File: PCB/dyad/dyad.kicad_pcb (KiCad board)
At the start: 2 copper layers, 7 parts, among them SW1 SW_SPST, SW2 SW_SPST, SW3 SW_SPST, SW4 SW_SPST, SW5 SW_SPST, SW6 SW_SPST

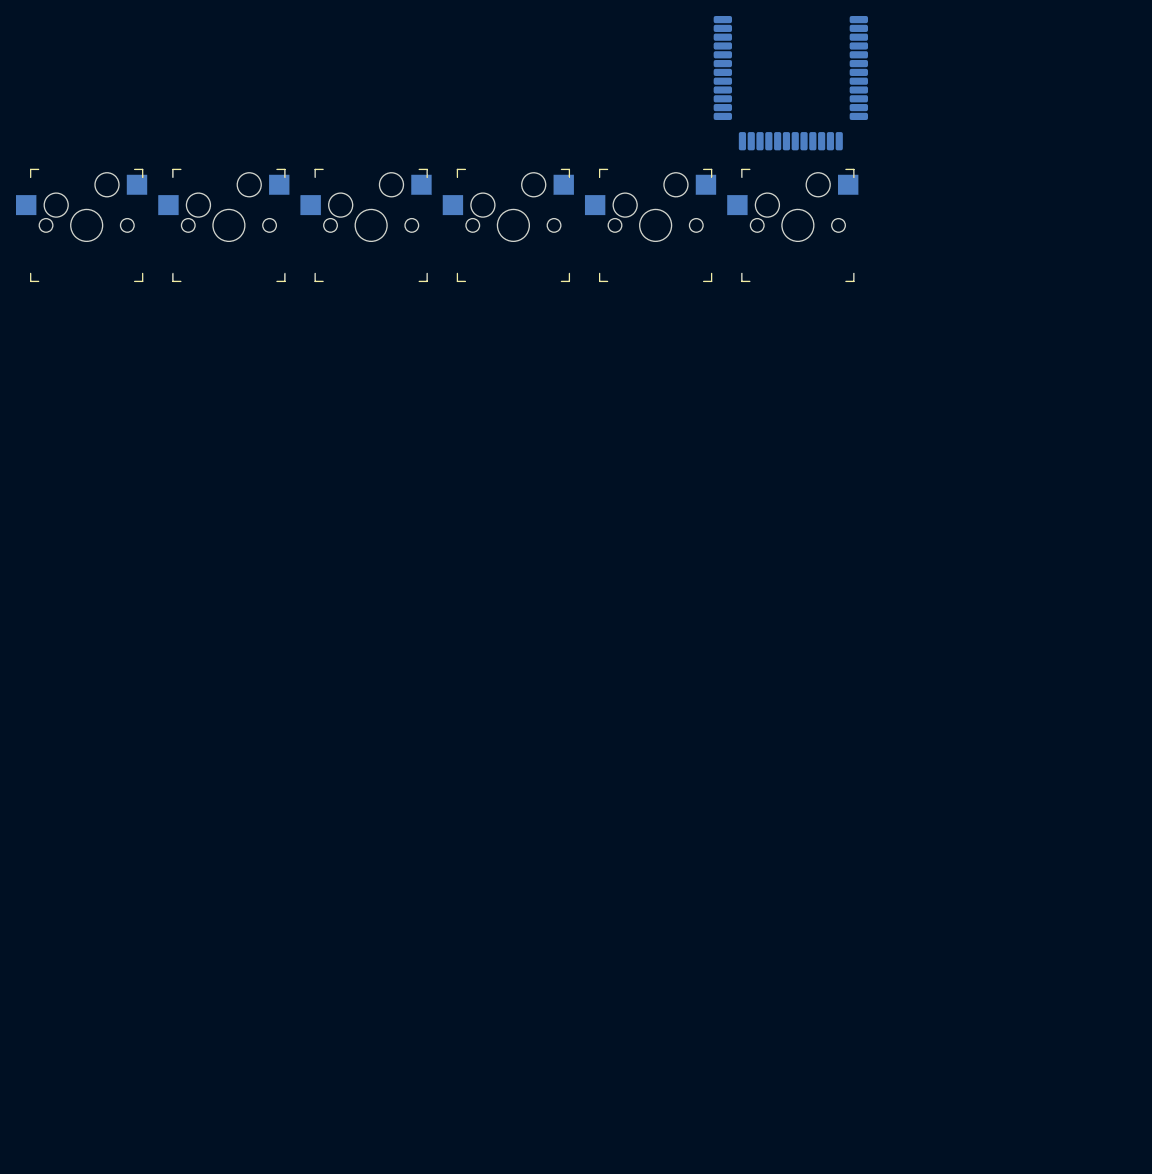
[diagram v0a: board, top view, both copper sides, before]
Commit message: add diodes
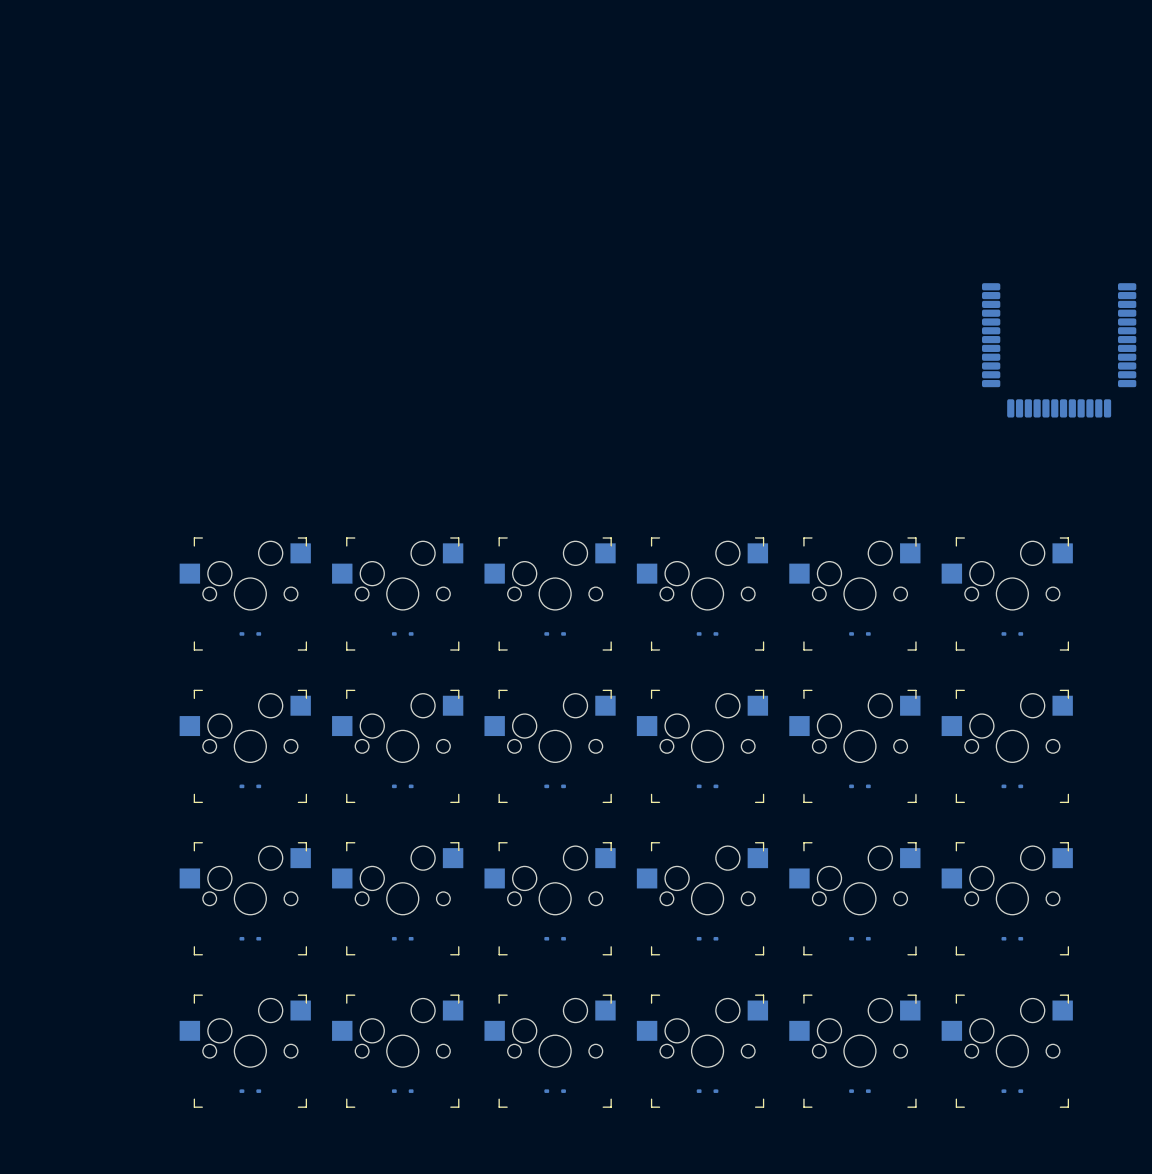
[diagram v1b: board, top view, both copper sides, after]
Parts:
- added D1: 1N4148WS, Diode_SMD:D_SOD-323, B.Cu at (48.4, 107.0)
- added D10: 1N4148WS, Diode_SMD:D_SOD-323, B.Cu at (105.5, 126.0)
- added D11: 1N4148WS, Diode_SMD:D_SOD-323, B.Cu at (124.6, 126.0)
- added D12: 1N4148WS, Diode_SMD:D_SOD-323, B.Cu at (143.7, 126.0)
- added D13: 1N4148WS, Diode_SMD:D_SOD-323, B.Cu at (48.4, 145.1)
- added D14: 1N4148WS, Diode_SMD:D_SOD-323, B.Cu at (67.5, 145.1)
- added D15: 1N4148WS, Diode_SMD:D_SOD-323, B.Cu at (86.5, 145.1)
- added D16: 1N4148WS, Diode_SMD:D_SOD-323, B.Cu at (105.5, 145.1)
- added D17: 1N4148WS, Diode_SMD:D_SOD-323, B.Cu at (124.6, 145.1)
- added D18: 1N4148WS, Diode_SMD:D_SOD-323, B.Cu at (143.7, 145.1)
- added D19: 1N4148WS, Diode_SMD:D_SOD-323, B.Cu at (48.4, 164.1)
- added D2: 1N4148WS, Diode_SMD:D_SOD-323, B.Cu at (67.5, 107.0)
- added D20: 1N4148WS, Diode_SMD:D_SOD-323, B.Cu at (67.5, 164.1)
- added D21: 1N4148WS, Diode_SMD:D_SOD-323, B.Cu at (86.5, 164.1)
- added D22: 1N4148WS, Diode_SMD:D_SOD-323, B.Cu at (105.5, 164.1)
- added D23: 1N4148WS, Diode_SMD:D_SOD-323, B.Cu at (124.6, 164.1)
- added D24: 1N4148WS, Diode_SMD:D_SOD-323, B.Cu at (143.7, 164.1)
- added D3: 1N4148WS, Diode_SMD:D_SOD-323, B.Cu at (86.5, 107.0)
- added D4: 1N4148WS, Diode_SMD:D_SOD-323, B.Cu at (105.5, 107.0)
- added D5: 1N4148WS, Diode_SMD:D_SOD-323, B.Cu at (124.6, 107.0)
- added D6: 1N4148WS, Diode_SMD:D_SOD-323, B.Cu at (143.7, 107.0)
- added D7: 1N4148WS, Diode_SMD:D_SOD-323, B.Cu at (48.4, 126.0)
- added D8: 1N4148WS, Diode_SMD:D_SOD-323, B.Cu at (67.5, 126.0)
- added D9: 1N4148WS, Diode_SMD:D_SOD-323, B.Cu at (86.5, 126.0)
- added SW10: SW_SPST, keyswitches.pretty-master:Kailh_socket_MX, F.Cu at (105.5, 121.0)
- added SW11: SW_SPST, keyswitches.pretty-master:Kailh_socket_MX, F.Cu at (124.6, 121.0)
- added SW12: SW_SPST, keyswitches.pretty-master:Kailh_socket_MX, F.Cu at (143.7, 121.0)
- added SW13: SW_SPST, keyswitches.pretty-master:Kailh_socket_MX, F.Cu at (48.4, 140.1)
- added SW14: SW_SPST, keyswitches.pretty-master:Kailh_socket_MX, F.Cu at (67.5, 140.1)
- added SW15: SW_SPST, keyswitches.pretty-master:Kailh_socket_MX, F.Cu at (86.5, 140.1)
- added SW16: SW_SPST, keyswitches.pretty-master:Kailh_socket_MX, F.Cu at (105.5, 140.1)
- added SW17: SW_SPST, keyswitches.pretty-master:Kailh_socket_MX, F.Cu at (124.6, 140.1)
- added SW18: SW_SPST, keyswitches.pretty-master:Kailh_socket_MX, F.Cu at (143.7, 140.1)
- added SW19: SW_SPST, keyswitches.pretty-master:Kailh_socket_MX, F.Cu at (48.4, 159.1)
- added SW20: SW_SPST, keyswitches.pretty-master:Kailh_socket_MX, F.Cu at (67.5, 159.1)
- added SW21: SW_SPST, keyswitches.pretty-master:Kailh_socket_MX, F.Cu at (86.5, 159.1)
- added SW22: SW_SPST, keyswitches.pretty-master:Kailh_socket_MX, F.Cu at (105.5, 159.1)
- added SW23: SW_SPST, keyswitches.pretty-master:Kailh_socket_MX, F.Cu at (124.6, 159.1)
- added SW24: SW_SPST, keyswitches.pretty-master:Kailh_socket_MX, F.Cu at (143.7, 159.1)
- added SW7: SW_SPST, keyswitches.pretty-master:Kailh_socket_MX, F.Cu at (48.4, 121.0)
- added SW8: SW_SPST, keyswitches.pretty-master:Kailh_socket_MX, F.Cu at (67.5, 121.0)
- added SW9: SW_SPST, keyswitches.pretty-master:Kailh_socket_MX, F.Cu at (86.5, 121.0)
- moved SW6 53.3 mm to (143.7, 102.0)
- moved SW5 52.7 mm to (124.6, 102.0)
- moved SW4 52.1 mm to (105.5, 102.0)
- moved SW3 51.5 mm to (86.5, 102.0)
- moved SW2 50.9 mm to (67.5, 102.0)
- moved SW1 50.4 mm to (48.4, 102.0)
- moved U1 47.3 mm to (158.0, 78.8)
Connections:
- SW1 pad 1: unconnected-(SW1-A-Pad1) -> ROW0
- SW1 pad 2: unconnected-(SW1-B-Pad2) -> Net-(D1-A)
- SW2 pad 1: unconnected-(SW2-A-Pad1) -> ROW0
- SW2 pad 2: unconnected-(SW2-B-Pad2) -> Net-(D2-A)
- SW3 pad 1: unconnected-(SW3-A-Pad1) -> ROW0
- SW3 pad 2: unconnected-(SW3-B-Pad2) -> Net-(D3-A)
- SW4 pad 1: unconnected-(SW4-A-Pad1) -> ROW0
- SW4 pad 2: unconnected-(SW4-B-Pad2) -> Net-(D4-A)
- SW5 pad 1: unconnected-(SW5-A-Pad1) -> ROW0
- SW5 pad 2: unconnected-(SW5-B-Pad2) -> Net-(D5-A)
- SW6 pad 1: unconnected-(SW6-A-Pad1) -> ROW0
- SW6 pad 2: unconnected-(SW6-B-Pad2) -> Net-(D6-A)

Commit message: added mounting holes
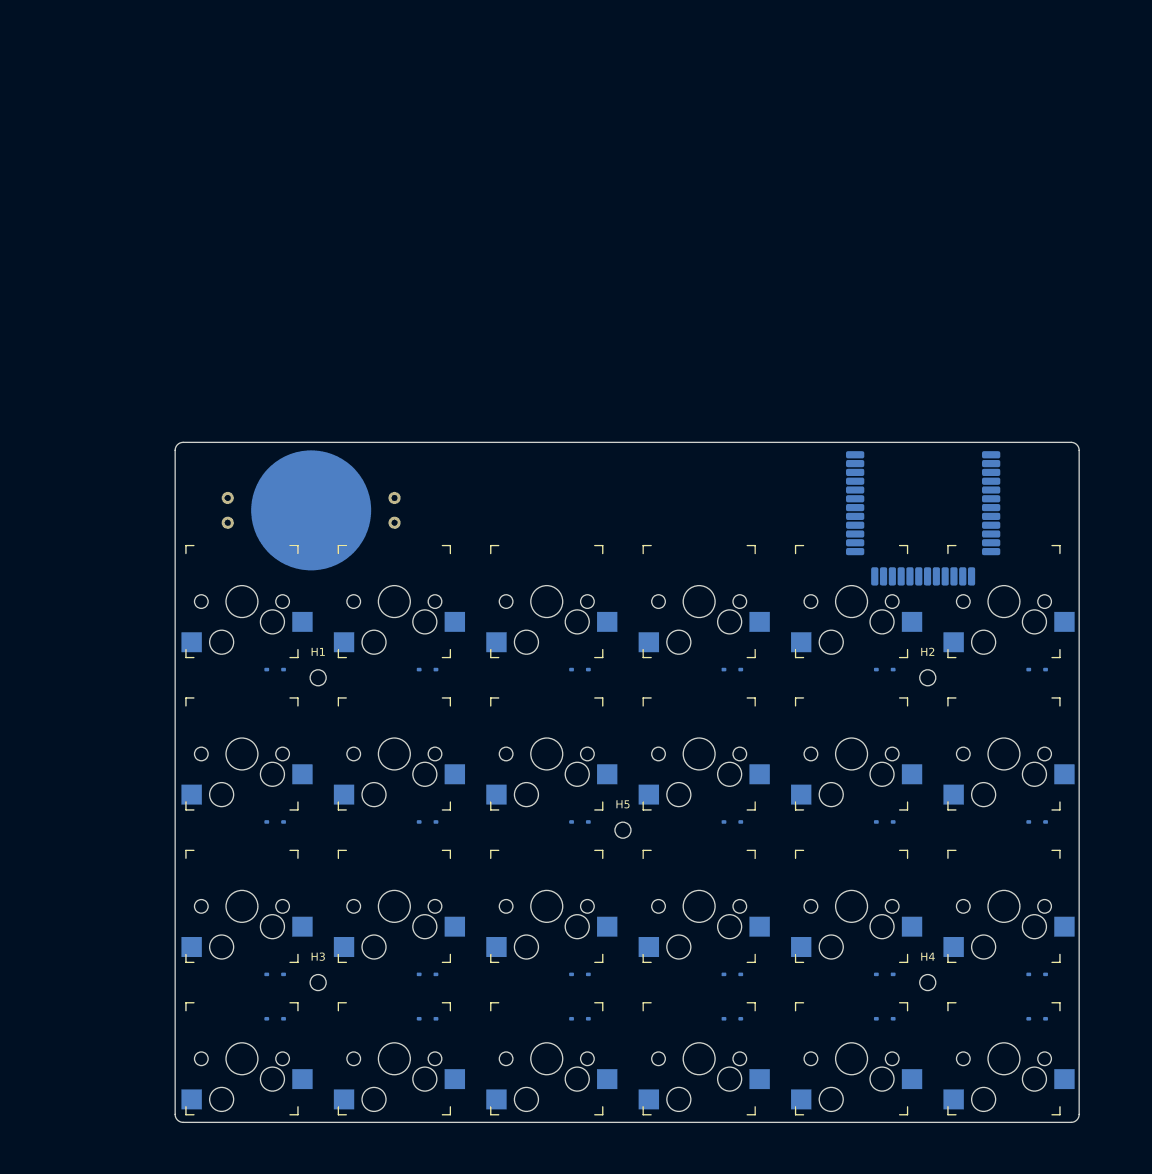
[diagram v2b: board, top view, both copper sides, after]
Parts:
- added BT1: Battery_Cell, lcsc:MY-2032-31, B.Cu at (56.0, 91.5)
- added H1: MountingHole, MountingHole:MountingHole_2mm, F.Cu at (56.9, 112.4)
- added H2: MountingHole, MountingHole:MountingHole_2mm, F.Cu at (133.1, 112.4)
- added H3: MountingHole, MountingHole:MountingHole_2mm, F.Cu at (56.9, 150.5)
- added H4: MountingHole, MountingHole:MountingHole_2mm, F.Cu at (133.1, 150.5)
- added H5: MountingHole, MountingHole:MountingHole_2mm, F.Cu at (95.0, 131.5)
- moved SW6 112.5 mm to (47.4, 160.1), turned to 180 degrees
- moved D19 111.6 mm to (146.8, 111.4), turned to 0 degrees
- moved SW24 111.5 mm to (47.4, 102.9), turned to 180 degrees
- moved SW1 110.7 mm to (142.6, 160.1), turned to 180 degrees
- moved SW19 109.7 mm to (142.6, 102.9), turned to 180 degrees
- moved D1 109.5 mm to (146.8, 155.1), turned to 0 degrees
- moved D24 106.2 mm to (51.5, 111.4), turned to 0 degrees
- moved D6 103.9 mm to (51.5, 155.1), turned to 0 degrees
- moved D7 101.1 mm to (146.8, 149.5), turned to 0 degrees
- moved D13 99.4 mm to (146.8, 130.4), turned to 0 degrees
- moved SW12 98.4 mm to (47.4, 141.0), turned to 180 degrees
- moved SW18 98.0 mm to (47.4, 122.0), turned to 180 degrees
- moved SW7 96.3 mm to (142.6, 141.0), turned to 180 degrees
- moved SW13 95.9 mm to (142.6, 122.0), turned to 180 degrees
- moved D12 95.1 mm to (51.5, 149.5), turned to 0 degrees
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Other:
- board outline added: 113 x 85 mm

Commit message: update pcb and schematic
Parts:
- added CHG1: Conn_01x04_Pin, Connector_PinHeader_2.54mm:PinHeader_1x04_P2.54mm_Vertical, F.Cu at (83.4, 88.8)
- added PRG1: Conn_01x04_Pin, Connector_PinHeader_2.54mm:PinHeader_1x04_P2.54mm_Vertical, F.Cu at (146.2, 85.8)
- moved BT1 1.09 mm to (56.9, 92.0)
- renumbered D24 to D1, D15 to D10, D14 to D11, D13 to D12, D12 to D13, D11 to D14, D10 to D15, D9 to D16, D8 to D17, D7 to D18, D6 to D19, D23 to D2, D5 to D20, D4 to D21, D3 to D22, D2 to D23, D1 to D24, D22 to D3, D21 to D4, D20 to D5, D19 to D6, D18 to D7, D17 to D8, D16 to D9, SW24 to SW1, SW15 to SW10, SW14 to SW11, SW13 to SW12, SW12 to SW13, SW11 to SW14, SW10 to SW15, SW9 to SW16, SW8 to SW17, SW7 to SW18, SW6 to SW19, SW23 to SW2, SW5 to SW20, SW4 to SW21, SW3 to SW22, SW2 to SW23, SW1 to SW24, SW22 to SW3, SW21 to SW4, SW20 to SW5, SW19 to SW6, SW18 to SW7, SW17 to SW8, SW16 to SW9
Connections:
- D1 pad 1: COL5 -> COL0
- D10 pad 1: COL2 -> COL3
- D11 pad 1: COL1 -> COL4
- D12 pad 1: COL0 -> COL5
- D13 pad 1: COL5 -> COL0
- D14 pad 1: COL4 -> COL1
- D15 pad 1: COL3 -> COL2
- D16 pad 1: COL2 -> COL3
- D17 pad 1: COL1 -> COL4
- D18 pad 1: COL0 -> COL5
- D19 pad 1: COL5 -> COL0
- D2 pad 1: COL4 -> COL1
- D20 pad 1: COL4 -> COL1
- D21 pad 1: COL3 -> COL2
- D22 pad 1: COL2 -> COL3
- D23 pad 1: COL1 -> COL4
- D24 pad 1: COL0 -> COL5
- D3 pad 1: COL3 -> COL2
- D4 pad 1: COL2 -> COL3
- D5 pad 1: COL1 -> COL4
- D6 pad 1: COL0 -> COL5
- D7 pad 1: COL5 -> COL0
- D8 pad 1: COL4 -> COL1
- D9 pad 1: COL3 -> COL2
- SW1 pad 1: ROW3 -> ROW0
- SW10 pad 1: ROW2 -> ROW1
- SW11 pad 1: ROW2 -> ROW1
- SW12 pad 1: ROW2 -> ROW1
- SW13 pad 1: ROW1 -> ROW2
- SW14 pad 1: ROW1 -> ROW2
- SW15 pad 1: ROW1 -> ROW2
- SW16 pad 1: ROW1 -> ROW2
- SW17 pad 1: ROW1 -> ROW2
- SW18 pad 1: ROW1 -> ROW2
- SW19 pad 1: ROW0 -> ROW3
- SW2 pad 1: ROW3 -> ROW0
- SW20 pad 1: ROW0 -> ROW3
- SW21 pad 1: ROW0 -> ROW3
- SW22 pad 1: ROW0 -> ROW3
- SW23 pad 1: ROW0 -> ROW3
- SW24 pad 1: ROW0 -> ROW3
- SW3 pad 1: ROW3 -> ROW0
- SW4 pad 1: ROW3 -> ROW0
- SW5 pad 1: ROW3 -> ROW0
- SW6 pad 1: ROW3 -> ROW0
- SW7 pad 1: ROW2 -> ROW1
- SW8 pad 1: ROW2 -> ROW1
- SW9 pad 1: ROW2 -> ROW1
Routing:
- net ROW1: track 0.00 -> 232.9 mm
- net ROW2: track 0.00 -> 192.5 mm
- net ROW3: track 0.00 -> 175.5 mm
- net ROW0: track 0.00 -> 141.0 mm
- net COL0: track 0.00 -> 134.1 mm, vias 0 -> 2
- net COL1: track 0.00 -> 114.1 mm, vias 0 -> 2
- net COL5: track 0.00 -> 95.4 mm, vias 0 -> 2
- net COL2: track 0.00 -> 94.6 mm, vias 0 -> 2
- net COL4: track 0.00 -> 78.0 mm, vias 0 -> 2
- net COL3: track 0.00 -> 74.8 mm, vias 0 -> 2
- net VCC: track 0.00 -> 68.0 mm
- net B+: track 0.00 -> 41.3 mm
- net SWDIO: track 0.00 -> 29.5 mm
- net SWCLK: track 0.00 -> 27.3 mm
- net B-: track 0.00 -> 22.7 mm
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- added copper zone on B.Cu, net GND
- added copper zone on F.Cu, net GND
